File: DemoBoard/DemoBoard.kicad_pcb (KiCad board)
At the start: 2 copper layers, 2 parts, among them J2 Conn_01x02, U101 ICM7555xP

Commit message: Inital layout
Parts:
- removed J2: Conn_01x02, Connector_Wire:SolderWire-1.5sqmm_1x02_P6mm_D1.7mm_OD3mm_Relief
- added D1(5.1V)101: 1N47xxA, Diode_THT:D_DO-41_SOD81_P10.16mm_Horizontal, F.Cu at (123.5, 63.8)
- added D1(5.1V)102: 1N47xxA, Diode_THT:D_DO-41_SOD81_P10.16mm_Horizontal, F.Cu at (123.5, 68.0)
- added G***: LOGO, thermocline:thermocline-logo, F.Cu at (126.5, 58.5)
- added G***: LOGO, thermocline:monk, F.Cu at (130.0, 82.5)
- added J101: Conn_Coaxial, thermocline:HL-BNC-KHDA, F.Cu at (105.5, 68.7)
- added J102: Conn_Coaxial, thermocline:HL-BNC-KHDA, F.Cu at (105.5, 82.8)
- added J103: Conn_Coaxial, thermocline:HL-BNC-KHDA, F.Cu at (145.0, 69.0)
- added J105: Conn_Coaxial, thermocline:HL-BNC-KHDA, F.Cu at (145.0, 83.1)
- added Q101: 2N3904, Package_TO_SOT_THT:TO-92_Inline, F.Cu at (116.6, 85.1)
- moved U101 34.2 mm to (116.2, 72.2)

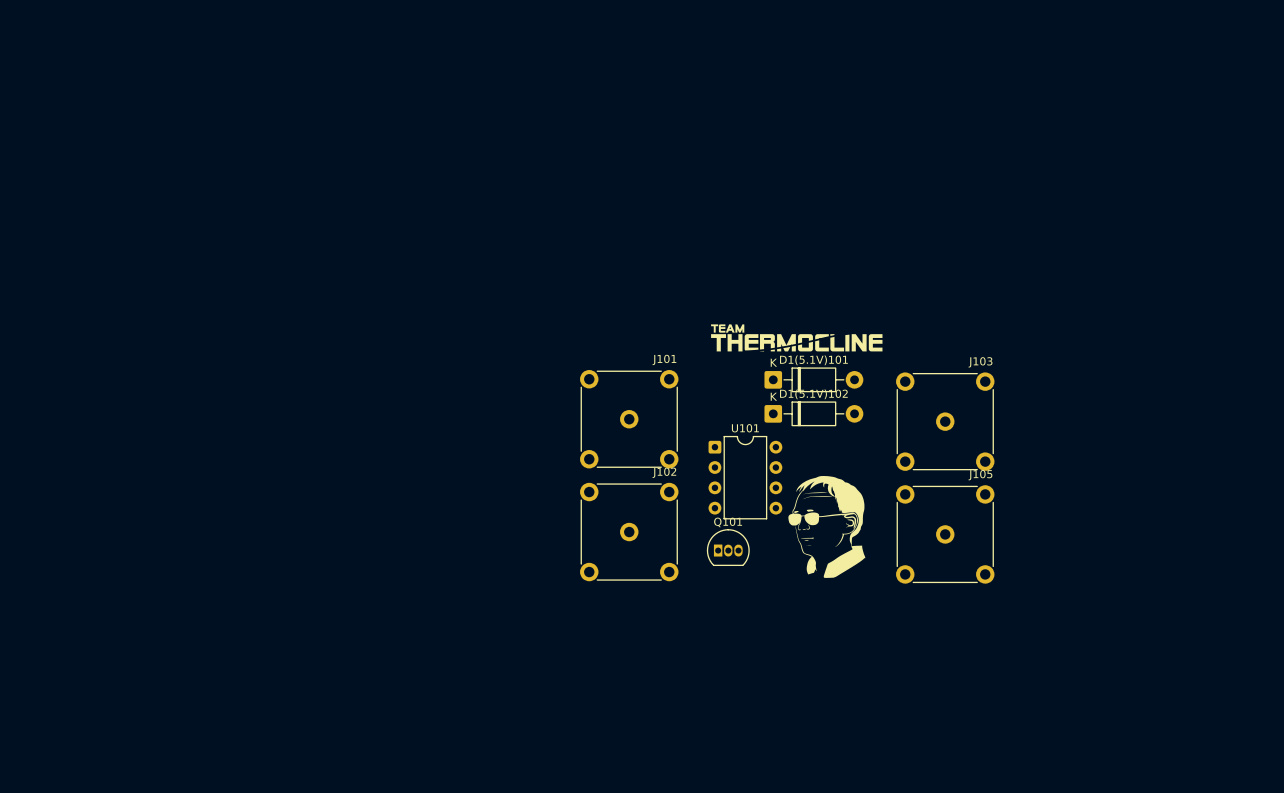
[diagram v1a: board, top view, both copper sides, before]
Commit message: Sectioned Everything on PCB
Drew Traces and such
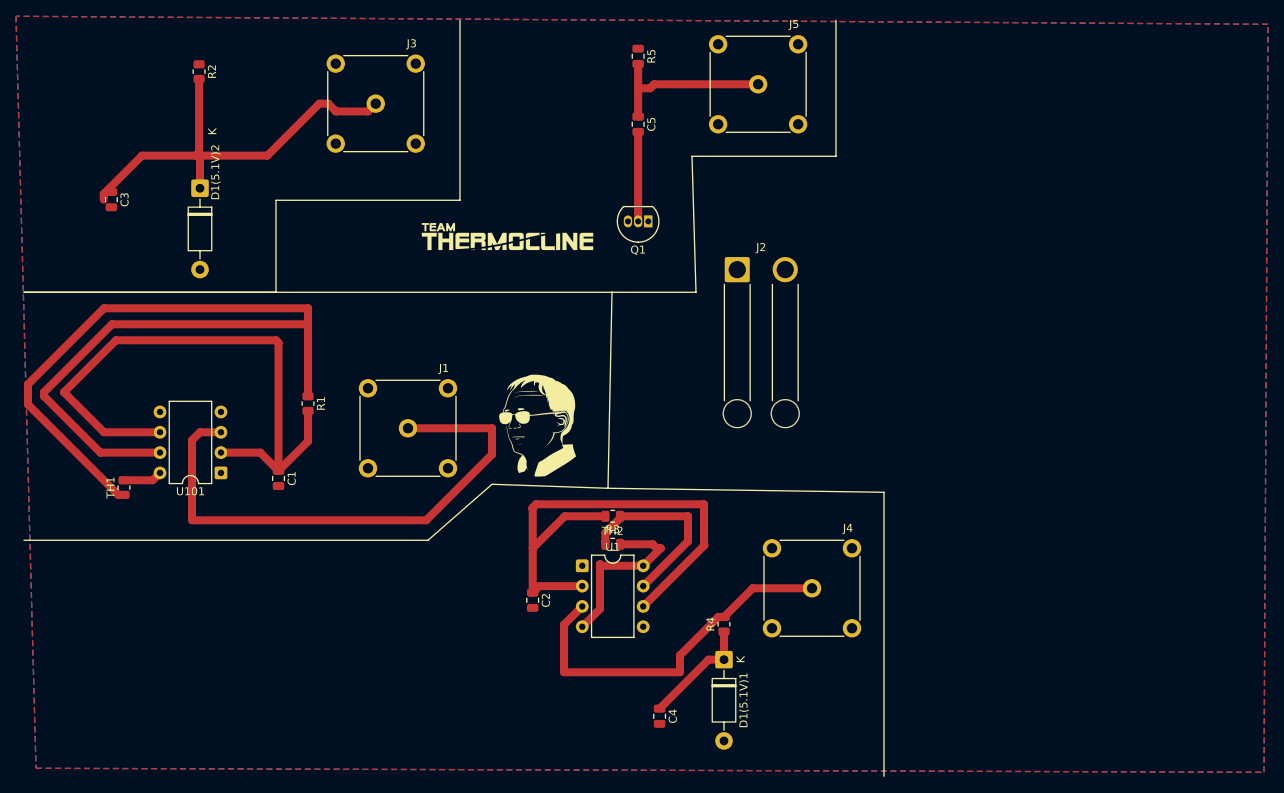
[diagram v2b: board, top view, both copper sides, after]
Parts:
- added C1: 1uF, Capacitor_SMD:C_0805_2012Metric, F.Cu at (61.7, 76.1)
- added C2: 1uF, Capacitor_SMD:C_0805_2012Metric, F.Cu at (93.4, 91.3)
- added C3: 1uF, Capacitor_SMD:C_0805_2012Metric, F.Cu at (40.8, 41.2)
- added C4: 1uF, Capacitor_SMD:C_0805_2012Metric, F.Cu at (109.3, 105.8)
- added C5: 0.1uF, Capacitor_SMD:C_0805_2012Metric, F.Cu at (106.6, 31.8)
- added J2: Conn_01x02, Connector_Wire:SolderWire-1.5sqmm_1x02_P6mm_D1.7mm_OD3mm_Relief, F.Cu at (119.0, 50.0)
- added R1: 100ko, Resistor_SMD:R_0805_2012Metric, F.Cu at (65.3, 66.7)
- added R2: 390o, Resistor_SMD:R_0805_2012Metric, F.Cu at (51.7, 25.2)
- added R3: 100ko, Resistor_SMD:R_0805_2012Metric, F.Cu at (103.4, 80.8)
- added R4: 2.2ko, Resistor_SMD:R_0805_2012Metric, F.Cu at (117.3, 94.3)
- added R5: 560ko, Capacitor_SMD:C_0805_2012Metric, F.Cu at (106.6, 23.3)
- added TH1: 10ko, Resistor_SMD:R_0805_2012Metric, F.Cu at (42.3, 77.2)
- added TH2: 10ko, Resistor_SMD:R_0805_2012Metric, F.Cu at (103.4, 84.3)
- added U101: ICM7555xP, Package_DIP:DIP-8_W7.62mm, F.Cu at (54.5, 75.4)
- moved D1(5.1V)2 75.6 mm to (51.8, 39.8), turned to -90 degrees
- moved J5 60.9 mm to (121.6, 26.8)
- moved J3 50.6 mm to (73.8, 29.2)
- moved Q1 42.1 mm to (107.9, 44.0), turned to 180 degrees
- moved G*** 38.3 mm to (90.3, 45.8)
- moved G*** 38.3 mm to (93.8, 69.8)
- moved D1(5.1V)1 31.3 mm to (117.3, 98.8), turned to -90 degrees
- moved J1 30.5 mm to (77.8, 69.8)
- moved J4 26.7 mm to (128.3, 89.8)
- moved U1 22.2 mm to (99.6, 87.0)
- renumbered D1(5.1V)102 to D1(5.1V)1, D1(5.1V)101 to D1(5.1V)2, J102 to J1, J101 to J3, J103 to J4, J105 to J5, Q101 to Q1, U101 to U1
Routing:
- net Net-(U101-DISCH): track 0.00 -> 123.6 mm
- net Net-(U101-THRES): track 0.00 -> 76.9 mm
- net Net-(J1-In): track 0.00 -> 68.7 mm
- net Net-(U1-THRES): track 0.00 -> 65.5 mm
- net Net-(D1(5.1V)2-K): track 0.00 -> 54.0 mm
- net Net-(J4-In): track 0.00 -> 45.8 mm
- net +9V: track 0.00 -> 27.5 mm
- net Net-(U1-DISCH): track 0.00 -> 23.8 mm
- net Net-(J5-In): track 0.00 -> 21.8 mm
- net Net-(D1(5.1V)1-K): track 0.00 -> 14.1 mm
- net Net-(Q1-B): track 0.00 -> 11.2 mm
- added copper zone on B.Cu, net +9V
- added copper zone on F.Cu, net GND
